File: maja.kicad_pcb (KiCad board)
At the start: 2 copper layers, 54 parts, among them J1 USB, K1 CONN_3, P1 JTAG, P2 CONN_8, SW1 RESET, SW2 BTN, SW3 BTN, U1 CC2538, U2 TPS70933, U3 Antenna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

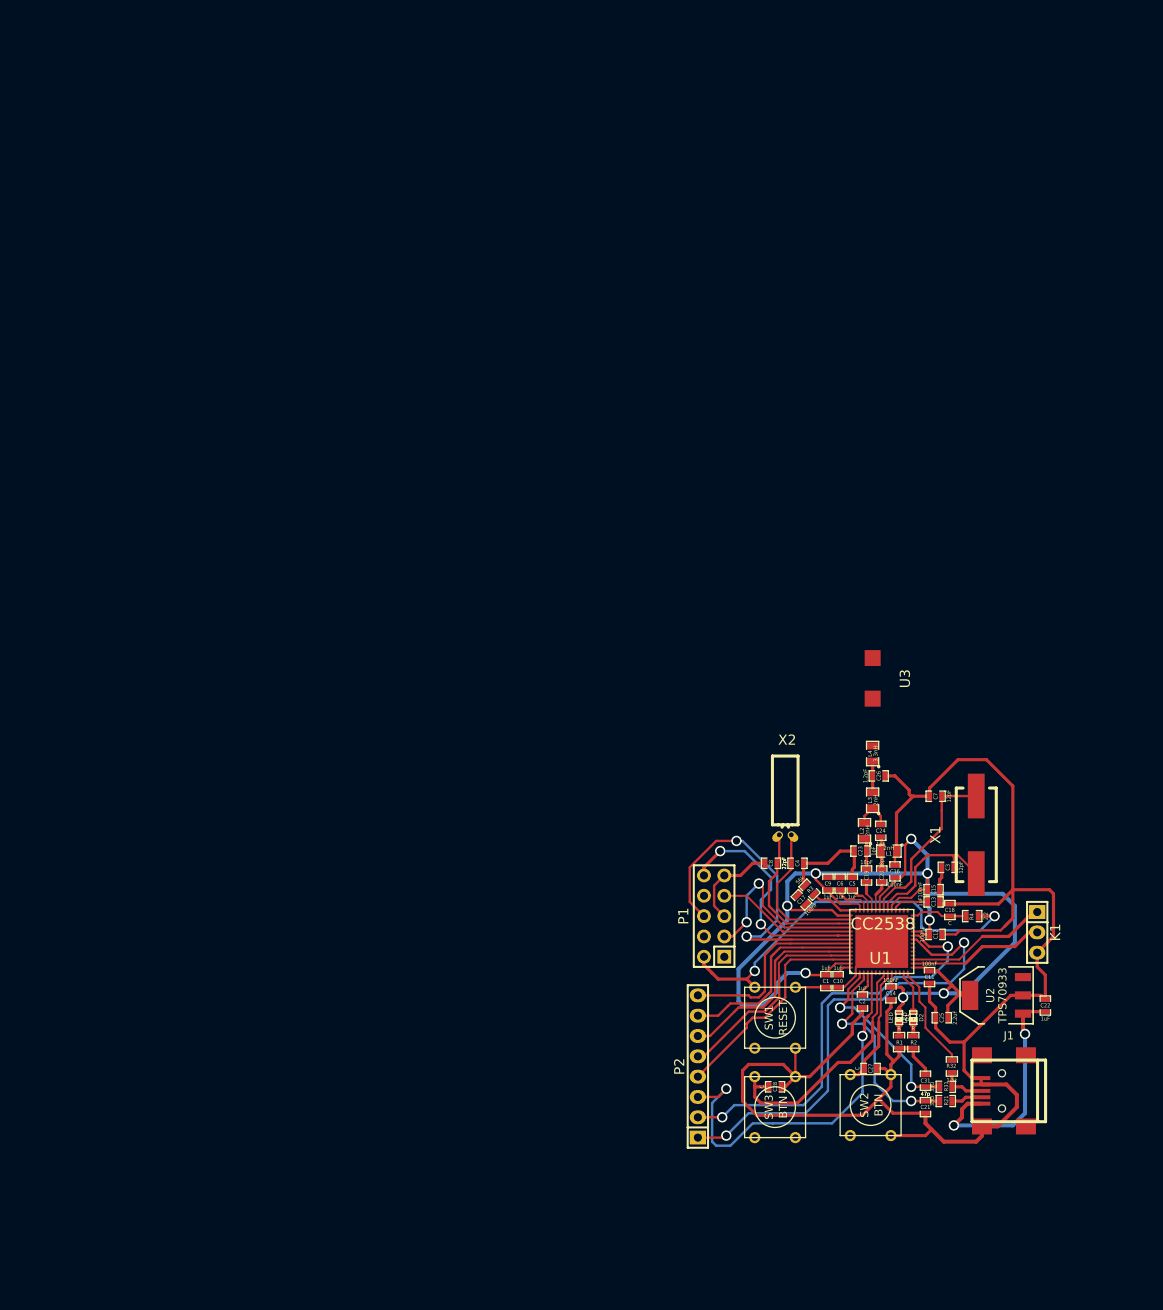
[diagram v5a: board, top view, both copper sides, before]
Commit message: Add antenna
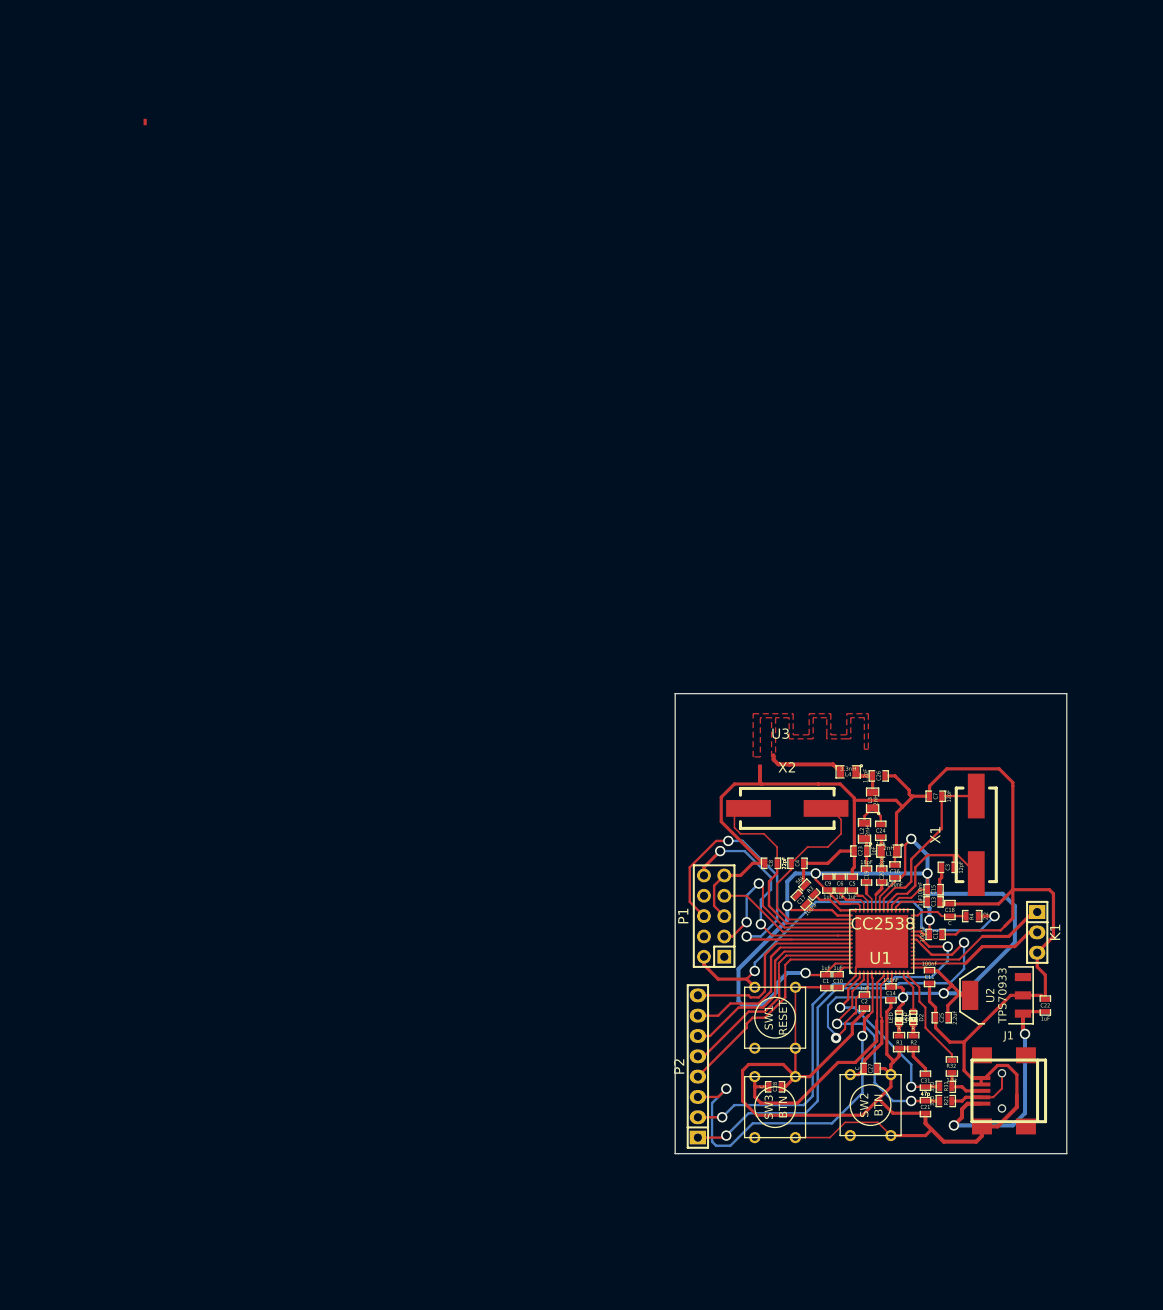
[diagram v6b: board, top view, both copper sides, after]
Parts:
- added STUB: VAL**, STUB, F.Cu at (0.00, 0.00)
- X2: footprint Crystals:Crystal_Round_Horizontal_3mm_BigPad -> Crystals:Crystal_HC49-SD_SMD
- moved U3 16.0 mm to (79.4, 80.4), turned to 180 degrees
- moved L4 3.82 mm to (87.9, 81.0), turned to 180 degrees
- moved X2 3.31 mm to (80.3, 85.6)
- moved C2 0.25 mm to (89.9, 109.7)
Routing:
- net GND: track 271.9 -> 338.1 mm
- net VDD: track 173.7 -> 195.7 mm, vias 8 -> 9
- net Net-(L4-Pad2): track 0.00 -> 9.56 mm
- net Net-(C8-Pad1): track 20.2 -> 28.8 mm
- net Net-(C4-Pad1): track 20.2 -> 28.6 mm
- net Net-(J1-Pad2): track 3.86 -> 8.82 mm
- net /USB_N: track 27.1 -> 28.0 mm
- net /JTAG_TDI: track 44.9 -> 44.3 mm
- net Net-(P2-Pad1): track 59.4 -> 60.0 mm
- net Net-(P2-Pad2): track 52.2 -> 52.8 mm
- added copper zone on F.Cu, net Net-(L4-Pad2)
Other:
- board outline added: 49 x 57.5 mm

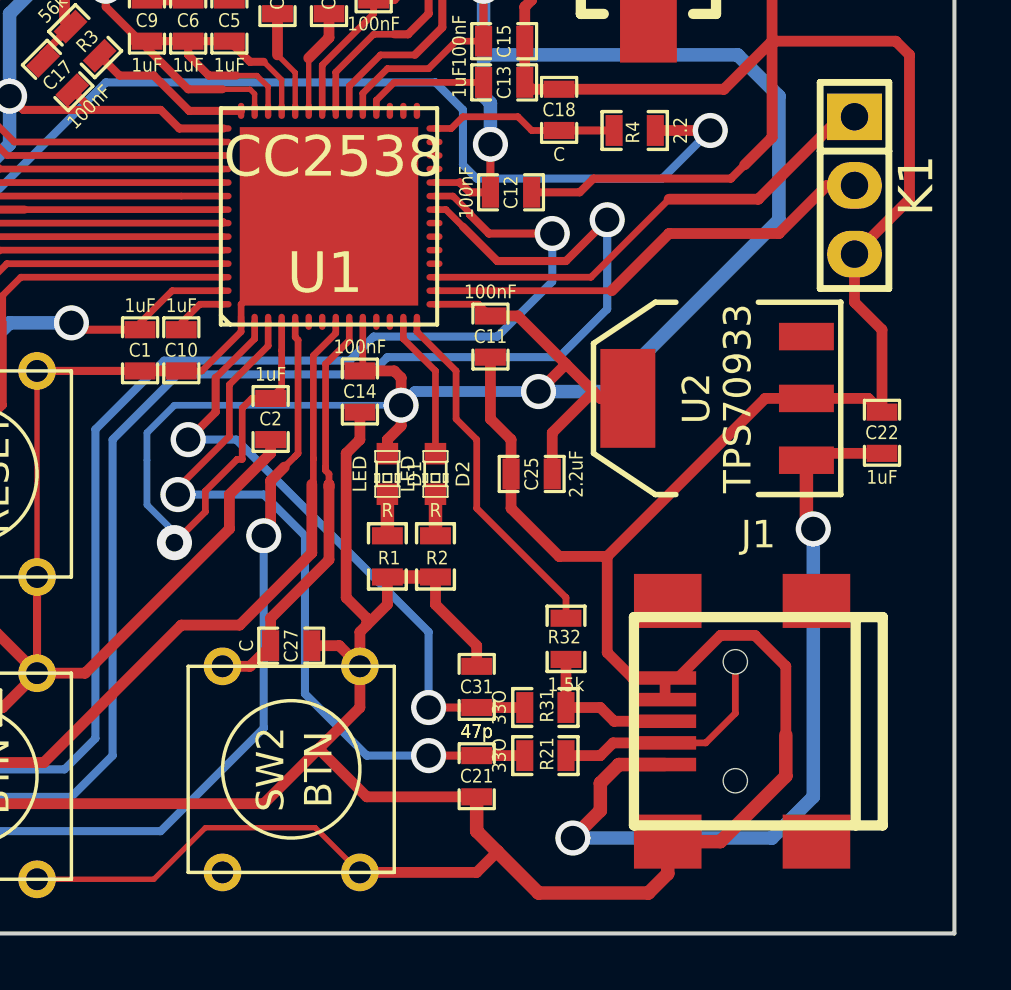
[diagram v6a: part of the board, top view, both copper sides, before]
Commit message: Get rid of 2 vias
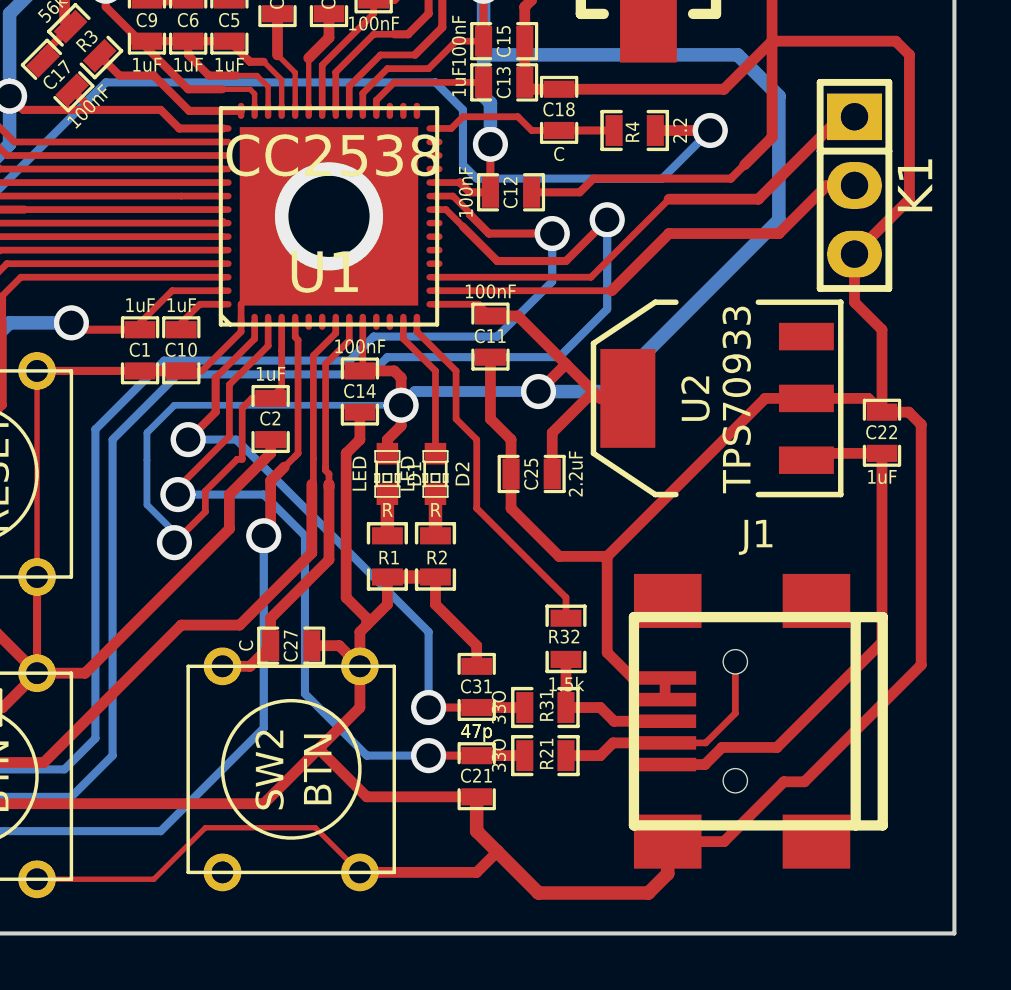
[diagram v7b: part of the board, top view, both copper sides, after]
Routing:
- net /V_USB: track 30.1 -> 19.8 mm, vias 2 -> 0
- net GND: track 338.1 -> 346.3 mm, vias 0 -> 1

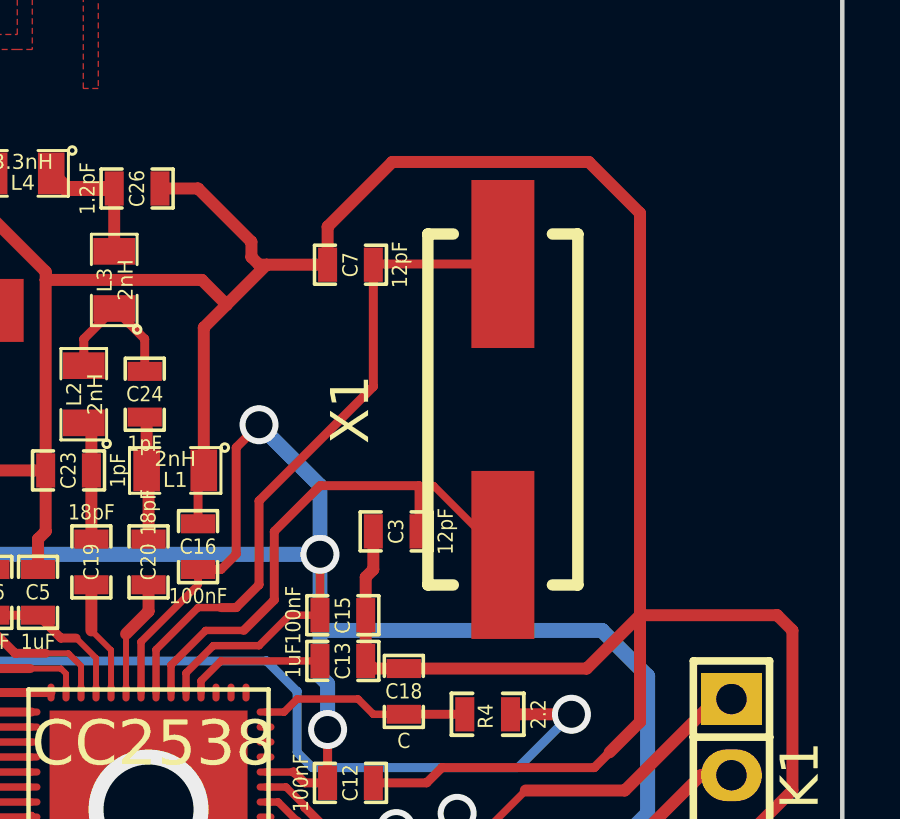
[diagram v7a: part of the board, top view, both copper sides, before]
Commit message: Change quartz
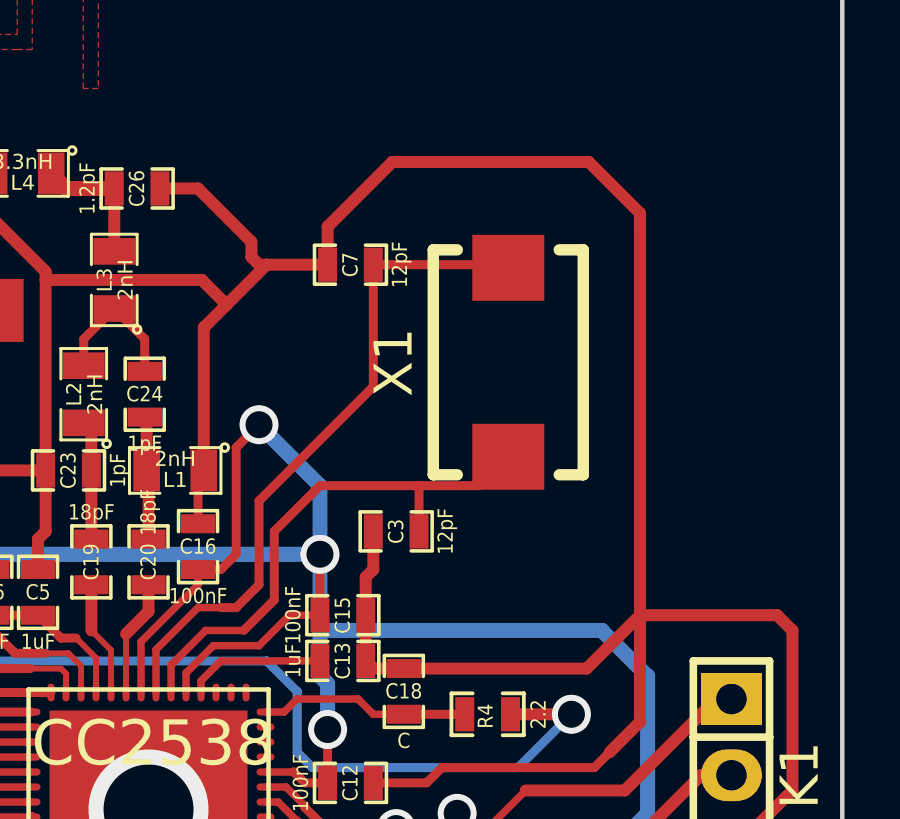
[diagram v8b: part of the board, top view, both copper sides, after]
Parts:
- X1: footprint Crystals:Crystal_HC49-SD_SMD -> Crystals:Crystal_FOX-FE_SMD
- moved X1 1.58 mm to (104.1, 87.3)
